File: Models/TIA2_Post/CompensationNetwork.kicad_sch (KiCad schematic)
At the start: 0 parts

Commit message: Finished with the chips for the transimpedance amplifiers
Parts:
- added C3: 2 nF, 1%, TwoTerminal:CAPC0603, symbol Device:C
- added C4: 180 pF, 1%, TwoTerminal:CAPC0603, symbol Device:C
- added R3: 1.3k, 1%, TwoTerminal:RESC0603, symbol Device:R_US
- added R4: 10k, 10%, ThreeTerminal:Bourns_3296Y, symbol Device:R_Potentiometer_US
- added R5: 200k, 10%, ThreeTerminal:Bourns_3296Y, symbol Device:R_Potentiometer_US
- added R6: 47k, 10%, ThreeTerminal:Bourns_3296Y, symbol Device:R_Potentiometer_US
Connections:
- new net: C3.2, R3.1
- new net: C4.1, R5.1, R5.2
- new net: R3.2, R4.3
- new net GND: R4.1, R4.2
- new net PostVoltage: C4.2, R6.1, R6.2
- new net PreVoltage: C3.1, R5.3, R6.3

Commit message: Save progress
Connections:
- net GND renamed ISO_GND
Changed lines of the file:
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@@
+		)
+	)
+	(global_label "ISO_GND"
+		(shape bidirectional)
+		(at 101.6 101.6 270)
+		(fields_autoplaced yes)
+		(effects
+			(font
+				(size 1.27 1.27)
+			)
+			(justify right)
+		)
+		(property "Intersheetrefs" "${INTERSHEET_REFS}"
+			(at 101.6 113.6794 90)
+			(effects
+				(font
+					(size 1.27 1.27)
+				)
+				(justify right)
+				(hide yes)
+			)
 		)
 	)
@@
 					(unit 1)
 				)
-			)
-		)
-	)
-	(symbol
-		(lib_id "power:GND")
-		(at 101.6 101.6 0)
-		(unit 1)
-		(exclude_from_sim no)
-		(in_bom yes)
-		(on_board yes)
-		(dnp no)
-		(fields_autoplaced yes)
-		(property "Reference" "#PWR04"
-			(at 101.6 107.95 0)
-			(effects
-				(font
-					(size 1.27 1.27)
-				)
-				(hide yes)
-			)
-		)
-		(property "Value" "GND"
-			(at 101.6 106.68 0)
-			(effects
-				(font
-					(size 1.27 1.27)
-				)
-			)
-		)
-		(property "Footprint" ""
-			(at 101.6 101.6 0)
-			(effects
-				(font
-					(size 1.27 1.27)
-				)
-				(hide yes)
-			)
-		)
-		(property "Datasheet" ""
-			(at 101.6 101.6 0)
-			(effects
-				(font
-					(size 1.27 1.27)
-				)
-				(hide yes)
-			)
-		)
-		(property "Description" "Power symbol creates a global label with name \"GND\" , ground"
-			(at 101.6 101.6 0)
-			(effects
-				(font
-					(size 1.27 1.27)
-				)
-				(hide yes)
-			)
-		)
-		(pin "1"
-		)
-		(instances
-			(project "TIA2_Post"
-				(path "/f19129fc-f916-4692-924c-ee308c6b3e1d/d4675321-04be-4323-a412-5fd261d625ce"
-					(reference "#PWR04")
-					(unit 1)
-				)

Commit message: Save progress
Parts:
- removed C4: 180 pF, 1%, TwoTerminal:CAPC0603, symbol Device:C
- removed R6: 47k, 10%, ThreeTerminal:Bourns_3296Y, symbol Device:R_Potentiometer_US
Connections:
- net PostVoltage: now also R5.1, R5.2
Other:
- moved on the sheet: R5

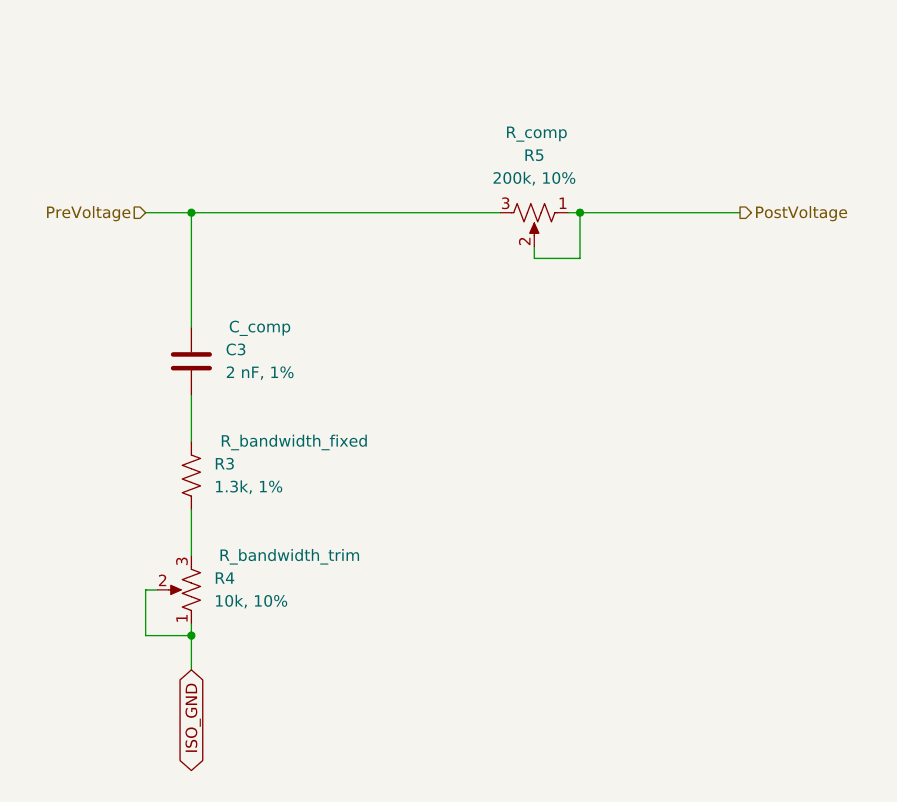
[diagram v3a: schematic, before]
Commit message: ERC passes for the two new boards
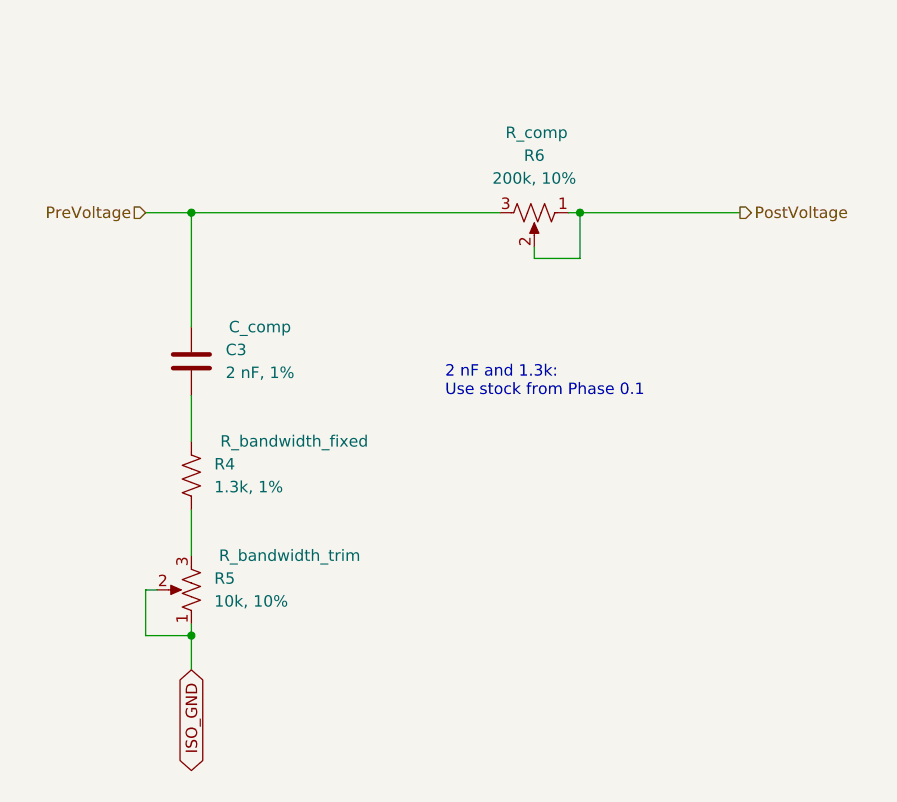
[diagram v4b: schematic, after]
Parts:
- C3: Purchase Link https://www.digikey.com/en/products/detail/murata-electroni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 -> (none); now left out of the parts list
- R4: renamed from R3; Purchase Link https://www.digikey.com/en/products/detail/vishay-dale/CRCW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 -> (none); now left out of the parts list
- R5: renamed from R4; Cost (none) -> $2.050
- R6: renamed from R5; Cost (none) -> $2.390
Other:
- note added: "2 nF and 1.3k: Use stock from Phase 0.1"
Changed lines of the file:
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@@
 	(generator_version "9.0")
 	(paper "A4")
+	(text "2 nF and 1.3k:\nUse stock from Phase 0.1"
+		(exclude_from_sim no)
+		(at 129.794 67.818 0)
+		(effects
+			(font
+				(size 1.27 1.27)
+			)
+			(justify left top)
+		)
+	)
 	(junction
 		(at 101.6 50.8)
@@
 		(unit 1)
 		(exclude_from_sim no)
-		(in_bom yes)
+		(in_bom no)
 		(on_board yes)
 		(dnp no)
@@
 			)
 		)
-		(property "Purchase Link" "https://www.digikey.com/en/products/detail/murata-electronics/GCM1885C1H202FA16D/16033535"
+		(property "Purchase Link" ""
 			(at 101.6 67.31 0)
 			(effects
@@
 		(on_board yes)
 		(dnp no)
-		(property "Reference" "R5"
+		(property "Reference" "R6"
 			(at 139.7 44.45 90)
 			(effects
@@
 		(property "Purchase Link" "https://www.digikey.com/en/products/detail/bourns-inc/3296Y-1-204LF/1088092"
 			(at 139.7 50.8 0)
+			(effects
+				(font
+					(size 1.27 1.27)
+				)
+				(hide yes)
+			)
+		)
+		(property "Cost" "$2.390"
+			(at 139.7 50.8 90)
 			(effects
 				(font
@@
 			(project "TIA2_Post"
 				(path "/f19129fc-f916-4692-924c-ee308c6b3e1d/d4675321-04be-4323-a412-5fd261d625ce"
-					(reference "R5")
+					(reference "R6")
 					(unit 1)
 				)
@@
 		(unit 1)
 		(exclude_from_sim no)
-		(in_bom yes)
+		(in_bom no)
 		(on_board yes)
 		(dnp no)
-		(property "Reference" "R3"
+		(property "Reference" "R4"
 			(at 104.14 78.7399 0)
 			(effects
@@
 			)
 		)
-		(property "Purchase Link" "https://www.digikey.com/en/products/detail/vishay-dale/CRCW06031K30FKEA/1174680"
+		(property "Purchase Link" ""
 			(at 101.6 80.01 0)
 			(effects
@@
 			(project "TIA2_Post"
 				(path "/f19129fc-f916-4692-924c-ee308c6b3e1d/d4675321-04be-4323-a412-5fd261d625ce"
-					(reference "R3")
+					(reference "R4")
 					(unit 1)
 				)
@@
 		(on_board yes)
 		(dnp no)
-		(property "Reference" "R4"
+		(property "Reference" "R5"
 			(at 104.14 91.4399 0)
 			(effects
@@
 		)
 		(property "Purchase Link" "https://www.digikey.com/en/products/detail/bourns-inc/3296Y-1-103LF/1088085"
+			(at 101.6 92.71 0)
+			(effects
+				(font
+					(size 1.27 1.27)
+				)
+				(hide yes)
+			)
+		)
+		(property "Cost" "$2.050"
 			(at 101.6 92.71 0)
 			(effects
@@
 			(project "TIA2_Post"
 				(path "/f19129fc-f916-4692-924c-ee308c6b3e1d/d4675321-04be-4323-a412-5fd261d625ce"
-					(reference "R4")
+					(reference "R5")
 					(unit 1)
 				)

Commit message: First time that all PCBs are fully wired
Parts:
- renumbered R5 to RV1, R6 to RV2
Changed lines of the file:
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@@
 		(on_board yes)
 		(dnp no)
-		(property "Reference" "R6"
+		(property "Reference" "RV2"
 			(at 139.7 44.45 90)
 			(effects
@@
 			(project "TIA2_Post"
 				(path "/f19129fc-f916-4692-924c-ee308c6b3e1d/d4675321-04be-4323-a412-5fd261d625ce"
-					(reference "R6")
+					(reference "RV2")
 					(unit 1)
 				)
@@
 		(on_board yes)
 		(dnp no)
-		(property "Reference" "R5"
+		(property "Reference" "RV1"
 			(at 104.14 91.4399 0)
 			(effects
@@
 			(project "TIA2_Post"
 				(path "/f19129fc-f916-4692-924c-ee308c6b3e1d/d4675321-04be-4323-a412-5fd261d625ce"
-					(reference "R5")
+					(reference "RV1")
 					(unit 1)
 				)

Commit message: Save progress
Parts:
- RV1, RV2: now left out of the parts list
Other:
- note added: "2 nF, 1.3k, Trimpots: Use stock from Phase 0.1"
- note removed: "2 nF and 1.3k: Use stock from Phase 0.1"
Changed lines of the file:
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@@
 	(generator_version "9.0")
 	(paper "A4")
-	(text "2 nF and 1.3k:\nUse stock from Phase 0.1"
+	(text "2 nF, 1.3k, Trimpots:\nUse stock from Phase 0.1"
 		(exclude_from_sim no)
 		(at 129.794 67.818 0)
@@
 		(unit 1)
 		(exclude_from_sim no)
-		(in_bom yes)
+		(in_bom no)
 		(on_board yes)
 		(dnp no)
@@
 		(unit 1)
 		(exclude_from_sim no)
-		(in_bom yes)
+		(in_bom no)
 		(on_board yes)
 		(dnp no)
